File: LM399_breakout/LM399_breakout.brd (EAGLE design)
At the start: 21.6 x 29.8 mm, 15 parts, among them U1 LM399

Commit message: * Final touchups on LM399 breakout board, ready to order!
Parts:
- added U$1: (no value), ohw-logo:OSHW_8X150_NOTEXT
- JP1: value (none) -> VCC
- JP2, JP4: value (none) -> GND
- JP3: value (none) -> Zener
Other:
- outline, holes or cut-outs redrawn
- board text removed: "cut out"

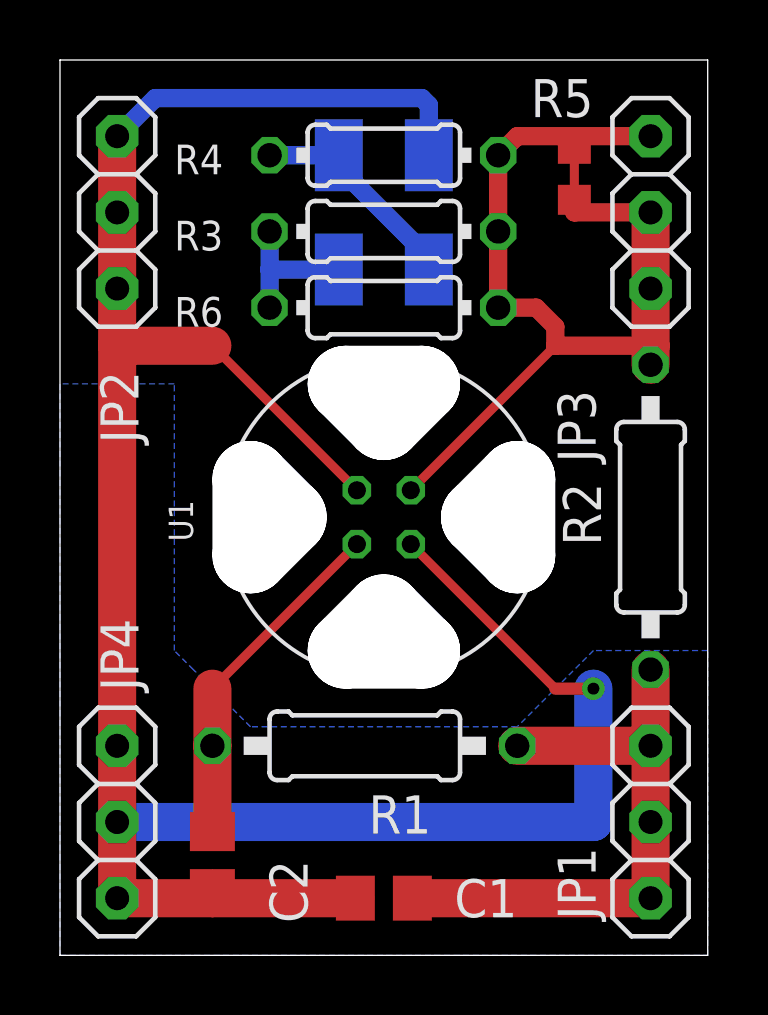
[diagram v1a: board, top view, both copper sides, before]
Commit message: * fixed mistakes with the lm399 board
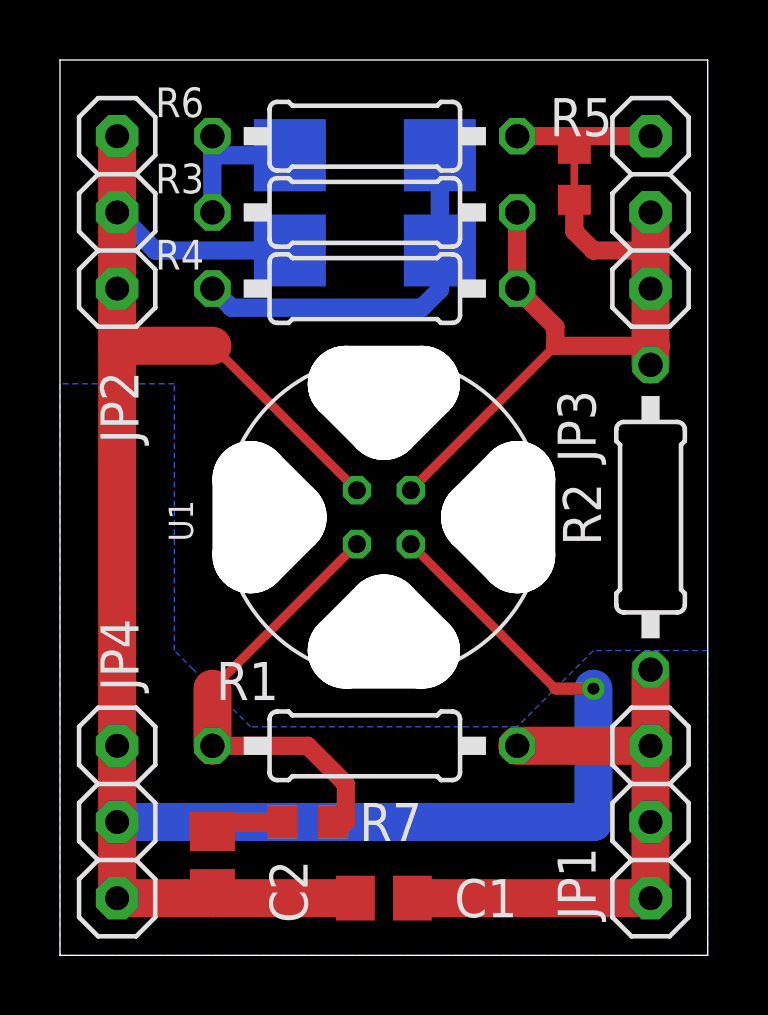
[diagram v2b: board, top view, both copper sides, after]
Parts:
- added R7: (no value), SquantorRCL:R0603
- C3, C4: device SquantorRCL:SMC_B -> SquantorRCL:SMC_C
- R3, R4, R6: device SquantorRCL:0204/7 -> SquantorRCL:0207/10
- moved R6 5.75 mm to (17.1, 27.9)
- moved R4 4.49 mm to (17.1, 22.9)
- moved C3 3.86 mm to (17.1, 27.3)
- moved C4 3.24 mm to (17.1, 24.1), turned to 0 degrees
- moved R3 0.90 mm to (17.1, 25.4)
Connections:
- new net N$2: C2.1, R7.2
- net N$1: now also R7.1; no longer C2.1
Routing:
- net GND: track 84.7 -> 78.3 mm
- net N$5: track 7.36 -> 12.6 mm
- net N$1: track 11.6 -> 15.4 mm
- net ZENER: track 33.0 -> 30.5 mm
- net N$2: track 0.00 -> 2.46 mm
